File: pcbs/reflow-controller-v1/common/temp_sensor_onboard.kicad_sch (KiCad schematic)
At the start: 3 parts, among them U1 TMP1075DSG

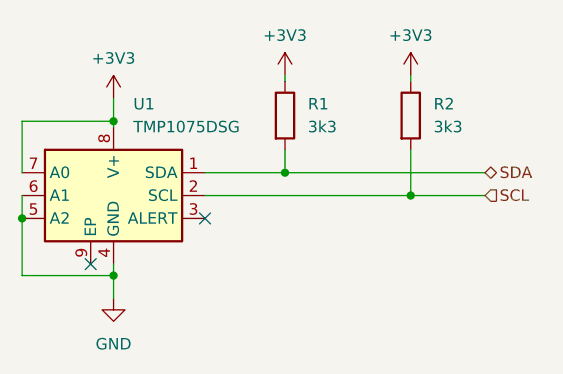
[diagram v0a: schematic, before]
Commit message: split pcbs into two for safety
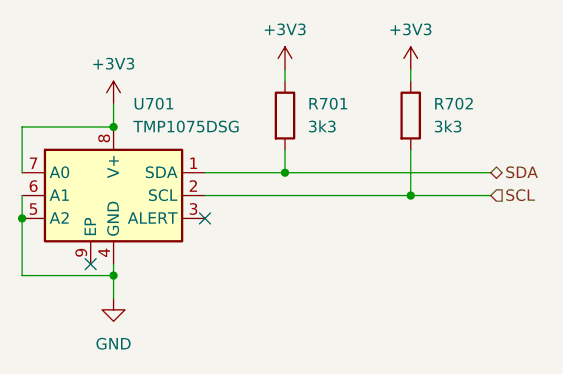
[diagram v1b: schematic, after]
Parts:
- renumbered R1 to R701, R2 to R702, U1 to U701
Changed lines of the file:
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@@
 (kicad_sch
-	(version 20231120)
+	(version 20250114)
 	(generator "eeschema")
-	(generator_version "8.0")
+	(generator_version "9.0")
 	(paper "A4")
 	(junction
@@
 	)
 	(junction
+		(at 140.97 81.28)
+		(diameter 0)
+		(color 0 0 0 0)
+	)
+	(junction
 		(at 173.99 88.9)
 		(diameter 0)
@@
 	)
 	(junction
-		(at 140.97 80.645)
-		(diameter 0)
-		(color 0 0 0 0)
-	)
-	(junction
 		(at 140.97 97.79)
 		(diameter 0)
@@
 	(wire
 		(pts
-			(xy 140.97 78.105) (xy 140.97 80.645)
-		)
-		(stroke
-			(width 0)
-			(type default)
-		)
-	)
-	(wire
-		(pts
-			(xy 140.97 80.645) (xy 140.97 81.28)
-		)
-		(stroke
-			(width 0)
-			(type default)
-		)
-	)
-	(wire
-		(pts
 			(xy 160.02 83.82) (xy 160.02 86.36)
 		)
@@
 	(wire
 		(pts
-			(xy 160.02 86.36) (xy 182.245 86.36)
-		)
-		(stroke
-			(width 0)
-			(type default)
-		)
-	)
-	(wire
-		(pts
-			(xy 160.02 75.565) (xy 160.02 76.2)
+			(xy 160.02 86.36) (xy 182.88 86.36)
+		)
+		(stroke
+			(width 0)
+			(type default)
+		)
+	)
+	(wire
+		(pts
+			(xy 160.02 74.93) (xy 160.02 76.2)
 		)
 		(stroke
@@
 	(wire
 		(pts
-			(xy 130.81 80.645) (xy 140.97 80.645)
-		)
-		(stroke
-			(width 0)
-			(type default)
-		)
-	)
-	(wire
-		(pts
-			(xy 173.99 75.565) (xy 173.99 76.2)
+			(xy 130.81 86.36) (xy 130.81 81.28)
+		)
+		(stroke
+			(width 0)
+			(type default)
+		)
+	)
+	(wire
+		(pts
+			(xy 173.99 74.93) (xy 173.99 76.2)
+		)
+		(stroke
+			(width 0)
+			(type default)
+		)
+	)
+	(wire
+		(pts
+			(xy 130.81 81.28) (xy 140.97 81.28)
+		)
+		(stroke
+			(width 0)
+			(type default)
+		)
+	)
+	(wire
+		(pts
+			(xy 140.97 78.74) (xy 140.97 81.28)
 		)
 		(stroke
@@
 	(wire
 		(pts
-			(xy 130.81 86.36) (xy 130.81 80.645)
-		)
-		(stroke
-			(width 0)
-			(type default)
-		)
-	)
-	(wire
-		(pts
 			(xy 173.99 83.82) (xy 173.99 88.9)
 		)
@@
 	(wire
 		(pts
-			(xy 173.99 88.9) (xy 182.245 88.9)
+			(xy 173.99 88.9) (xy 182.88 88.9)
 		)
 		(stroke
@@
 	(hierarchical_label "SDA"
 		(shape bidirectional)
-		(at 182.245 86.36 0)
-		(fields_autoplaced yes)
+		(at 182.88 86.36 0)
 		(effects
 			(font
@@
 	(hierarchical_label "SCL"
 		(shape input)
-		(at 182.245 88.9 0)
-		(fields_autoplaced yes)
+		(at 182.88 88.9 0)
 		(effects
 			(font
@@
 	(symbol
 		(lib_id "power:+3V3")
-		(at 160.02 75.565 0)
+		(at 160.02 74.93 0)
 		(unit 1)
 		(exclude_from_sim no)
@@
 		(dnp no)
 		(fields_autoplaced yes)
-		(property "Reference" "#PWR05"
-			(at 160.02 79.375 0)
+		(property "Reference" "#PWR0703"
+			(at 160.02 78.74 0)
 			(effects
 				(font
@@
 		)
 		(property "Value" "+3V3"
-			(at 160.02 71.12 0)
+			(at 160.02 70.485 0)
 			(effects
 				(font
@@
 		)
 		(property "Footprint" ""
-			(at 160.02 75.565 0)
+			(at 160.02 74.93 0)
 			(effects
 				(font
@@
 		)
 		(property "Datasheet" ""
-			(at 160.02 75.565 0)
+			(at 160.02 74.93 0)
 			(effects
 				(font
@@
 		)
 		(property "Description" "Power symbol creates a global label with name \"+3V3\""
-			(at 160.02 75.565 0)
+			(at 160.02 74.93 0)
 			(effects
 				(font
@@
 		)
 		(instances
+			(project "ui"
+				(path "/2ced3b3e-2fc8-4776-88d1-4bcb3cd16514/9b6e6a2c-2811-4c36-bbd7-fbd63c94c7ee"
+					(reference "#PWR0703")
+					(unit 1)
+				)
+			)
 			(project "reflow-controller-v1"
 				(path "/843848ae-bf49-42cb-8f8b-76790d2e568d/34e546ab-bb22-4653-bb8c-eaca24077e54"
@@
 	(symbol
 		(lib_id "power:+3V3")
-		(at 173.99 75.565 0)
+		(at 173.99 74.93 0)
 		(unit 1)
 		(exclude_from_sim no)
@@
 		(dnp no)
 		(fields_autoplaced yes)
-		(property "Reference" "#PWR06"
-			(at 173.99 79.375 0)
+		(property "Reference" "#PWR0704"
+			(at 173.99 78.74 0)
 			(effects
 				(font
@@
 		)
 		(property "Value" "+3V3"
-			(at 173.99 71.12 0)
+			(at 173.99 70.485 0)
 			(effects
 				(font
@@
 		)
 		(property "Footprint" ""
-			(at 173.99 75.565 0)
+			(at 173.99 74.93 0)
 			(effects
 				(font
@@
 		)
 		(property "Datasheet" ""
-			(at 173.99 75.565 0)
+			(at 173.99 74.93 0)
 			(effects
 				(font
@@
 		)
 		(property "Description" "Power symbol creates a global label with name \"+3V3\""
-			(at 173.99 75.565 0)
+			(at 173.99 74.93 0)
 			(effects
 				(font
@@
 		)
 		(instances
+			(project "ui"
+				(path "/2ced3b3e-2fc8-4776-88d1-4bcb3cd16514/9b6e6a2c-2811-4c36-bbd7-fbd63c94c7ee"
+					(reference "#PWR0704")
+					(unit 1)
+				)
+			)
 			(project "reflow-controller-v1"
 				(path "/843848ae-bf49-42cb-8f8b-76790d2e568d/34e546ab-bb22-4653-bb8c-eaca24077e54"
@@
 		(dnp no)
 		(fields_autoplaced yes)
-		(property "Reference" "#PWR01"
+		(property "Reference" "#PWR0702"
 			(at 140.97 106.68 0)
 			(effects
@@
 		)
 		(instances
+			(project "ui"
+				(path "/2ced3b3e-2fc8-4776-88d1-4bcb3cd16514/9b6e6a2c-2811-4c36-bbd7-fbd63c94c7ee"
+					(reference "#PWR0702")
+					(unit 1)
+				)
+			)
 			(project "reflow-controller-v1"
 				(path "/843848ae-bf49-42cb-8f8b-76790d2e568d/34e546ab-bb22-4653-bb8c-eaca24077e54"
@@
 		(dnp no)
 		(fields_autoplaced yes)
-		(property "Reference" "R2"
+		(property "Reference" "R702"
 			(at 176.53 78.74 0)
 			(effects
@@
 		)
 		(instances
+			(project "ui"
+				(path "/2ced3b3e-2fc8-4776-88d1-4bcb3cd16514/9b6e6a2c-2811-4c36-bbd7-fbd63c94c7ee"
+					(reference "R702")
+					(unit 1)
+				)
+			)
 			(project "reflow-controller-v1"
 				(path "/843848ae-bf49-42cb-8f8b-76790d2e568d/34e546ab-bb22-4653-bb8c-eaca24077e54"
@@
 		(dnp no)
 		(fields_autoplaced yes)
-		(property "Reference" "R1"
+		(property "Reference" "R701"
 			(at 162.56 78.74 0)
 			(effects
@@
 		)
 		(instances
+			(project "ui"
+				(path "/2ced3b3e-2fc8-4776-88d1-4bcb3cd16514/9b6e6a2c-2811-4c36-bbd7-fbd63c94c7ee"
+					(reference "R701")
+					(unit 1)
+				)
+			)
 			(project "reflow-controller-v1"
 				(path "/843848ae-bf49-42cb-8f8b-76790d2e568d/34e546ab-bb22-4653-bb8c-eaca24077e54"
@@
 		(dnp no)
 		(fields_autoplaced yes)
-		(property "Reference" "U1"
+		(property "Reference" "U701"
 			(at 143.1641 78.74 0)
 			(effects
@@
 		)
 		(instances
+			(project "ui"
+				(path "/2ced3b3e-2fc8-4776-88d1-4bcb3cd16514/9b6e6a2c-2811-4c36-bbd7-fbd63c94c7ee"
+					(reference "U701")
+					(unit 1)
+				)
+			)
 			(project "reflow-controller-v1"
 				(path "/843848ae-bf49-42cb-8f8b-76790d2e568d/34e546ab-bb22-4653-bb8c-eaca24077e54"
@@
 	(symbol
 		(lib_id "power:+3V3")
-		(at 140.97 78.105 0)
+		(at 140.97 78.74 0)
 		(unit 1)
 		(exclude_from_sim no)
@@
 		(dnp no)
 		(fields_autoplaced yes)
-		(property "Reference" "#PWR02"
-			(at 140.97 81.915 0)
+		(property "Reference" "#PWR0701"
+			(at 140.97 82.55 0)
 			(effects
 				(font
@@
 		)
 		(property "Value" "+3V3"
-			(at 140.97 73.66 0)
+			(at 140.97 74.295 0)
 			(effects
 				(font
@@
 		)
 		(property "Footprint" ""
-			(at 140.97 78.105 0)
+			(at 140.97 78.74 0)
 			(effects
 				(font
@@
 		)
 		(property "Datasheet" ""
-			(at 140.97 78.105 0)
+			(at 140.97 78.74 0)
 			(effects
 				(font
@@
 		)
 		(property "Description" "Power symbol creates a global label with name \"+3V3\""
-			(at 140.97 78.105 0)
+			(at 140.97 78.74 0)
 			(effects
 				(font
@@
 		)
 		(instances
+			(project "ui"
+				(path "/2ced3b3e-2fc8-4776-88d1-4bcb3cd16514/9b6e6a2c-2811-4c36-bbd7-fbd63c94c7ee"
+					(reference "#PWR0701")
+					(unit 1)
+				)
+			)
 			(project "reflow-controller-v1"
 				(path "/843848ae-bf49-42cb-8f8b-76790d2e568d/34e546ab-bb22-4653-bb8c-eaca24077e54"
